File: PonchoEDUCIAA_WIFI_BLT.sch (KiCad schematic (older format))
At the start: 21 parts, among them J1 UART, SW1 Reset, SW2 Boot, U1 ESP32-WROOM

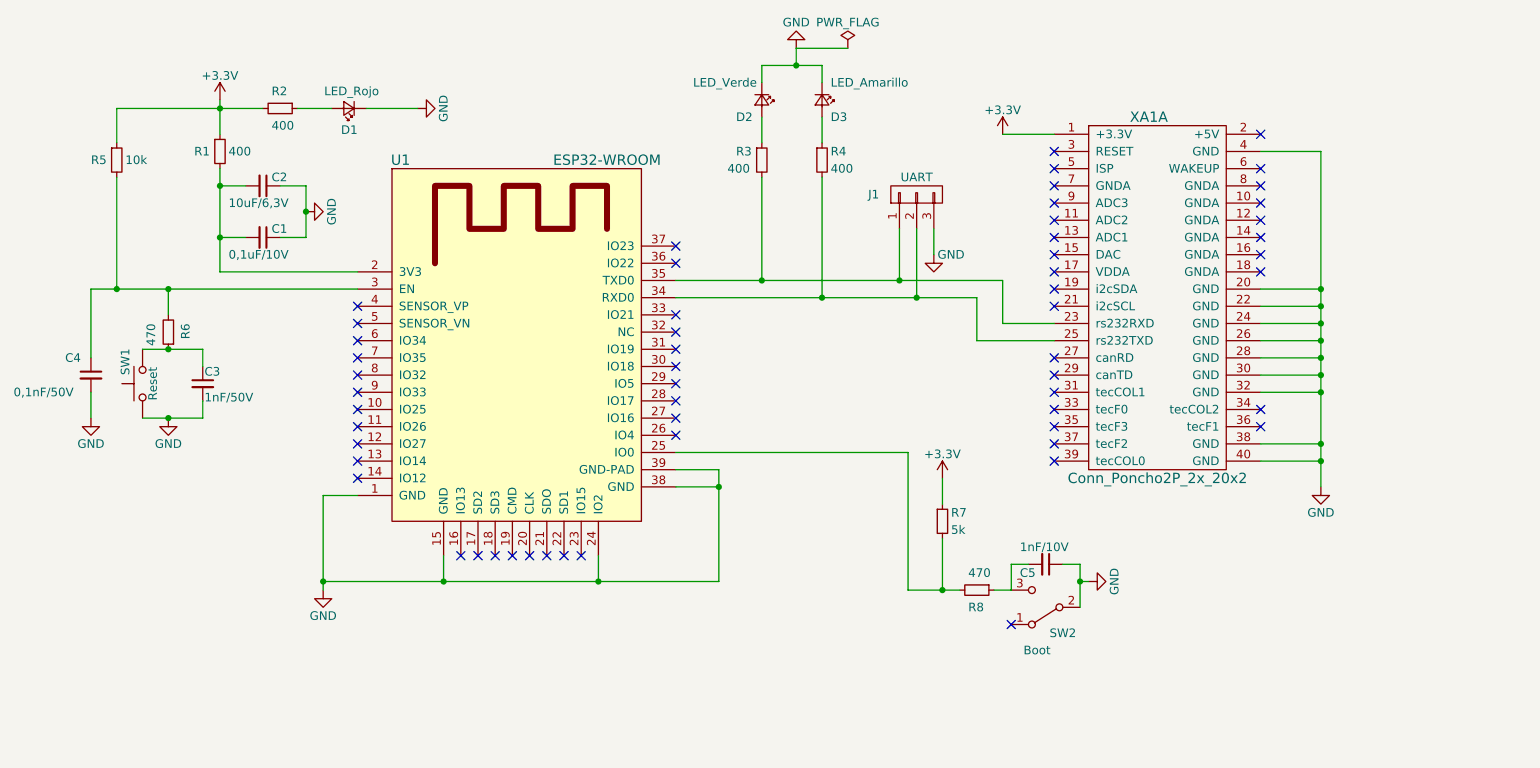
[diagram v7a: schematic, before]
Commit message: Se agregan modelos 3d al proyecto y datashets de algunos componentes
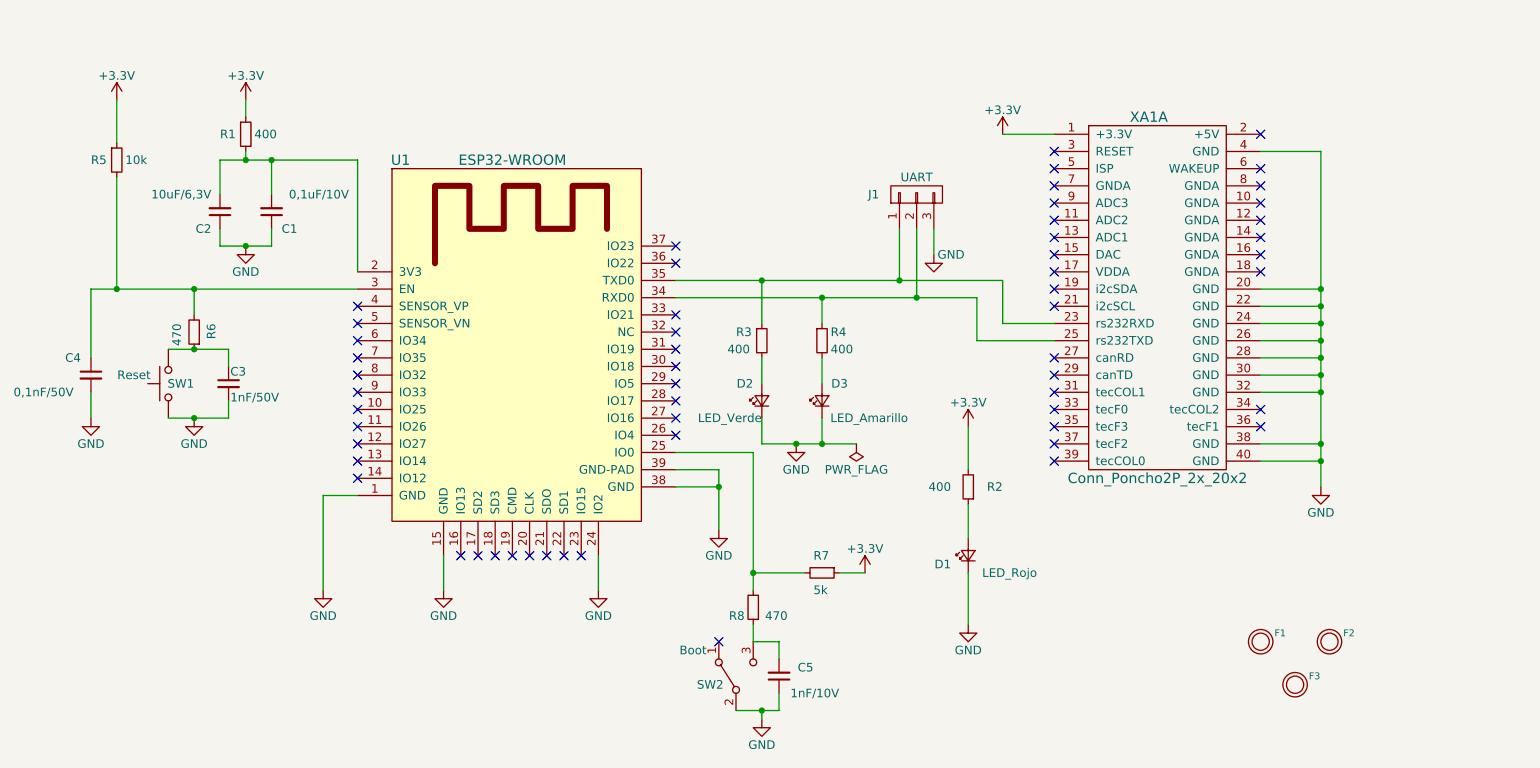
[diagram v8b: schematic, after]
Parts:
- added F1, F2, F3: FIDUCIAL, PonchoEDUCIAA_WIFI_BLTH:Fiducial_1mm, symbol FIDUCIAL
- C1: Desc (none) -> 0.1µF ±10% 6.3V Ceramic Capacitor X5R 0201 (0603 Metric); Digikey# (none) -> 478-5266-1-ND; Manf (none) -> AVX Corporation; Manf# (none) -> 02016D104KAT2A
- C2: Desc (none) -> 10µF ±10% 6.3V Ceramic Capacitor X5R 0805 (2012 Metric); Digikey# (none) -> 490-3340-1-ND; Manf (none) -> Murata Electronics North America; Manf# (none) -> GRM219R60J106KE19D
- C3: Desc (none) -> 100pF ±5% 50V Ceramic Capacitor C0G, NP0 0402 (1005 Metric); Digikey# (none) -> 490-5922-1-ND; Manf (none) -> Murata Electronics North America; Manf# (none) -> GRM1555C1H101JA01D
- C4: Desc (none) -> 10pF ±5% 50V Ceramic Capacitor C0G, NP0 0402 (1005 Metric); Digikey# (none) -> 490-5921-1-ND; Manf (none) -> Murata Electronics North America; Manf# (none) -> GRM1555C1H100JA01D
- C5: Desc (none) -> 100pF ±5% 10V Ceramic Capacitor C0G, NP0 0201 (0603 Metric); Digikey# (none) -> 478-1026-1-ND; Manf (none) -> AVX Corporation; Manf# (none) -> 0201ZA101JAT2A
- R5: Desc (none) -> 10k Ohm ±0.1% 0.063W, 1/16W Chip Resistor 0402 (1005 Metric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; Digikey# (none) -> A102579CT-ND; Manf (none) -> TE Connectivity Passive Product; Manf# (none) -> CPF0402B10KE1
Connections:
- net at J1.2 (P2), U1.34 (RXD0), XA1.25 (rs232TXD): now also R4.1; no longer R4.2
- net at J1.1 (P1), U1.35 (TXD0), XA1.23 (rs232RXD): now also R3.1; no longer R3.2
- net at D2.2 (A): now also R3.2; no longer R3.1
- net at D3.2 (A): now also R4.2; no longer R4.1
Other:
- moved on the sheet: C1, C2, C3, C5, D1, D2, D3, R1, R2, R3, R4, R6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
